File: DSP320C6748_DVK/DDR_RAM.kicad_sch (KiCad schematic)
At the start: 66 parts, among them IC13 W972GG6KB-25

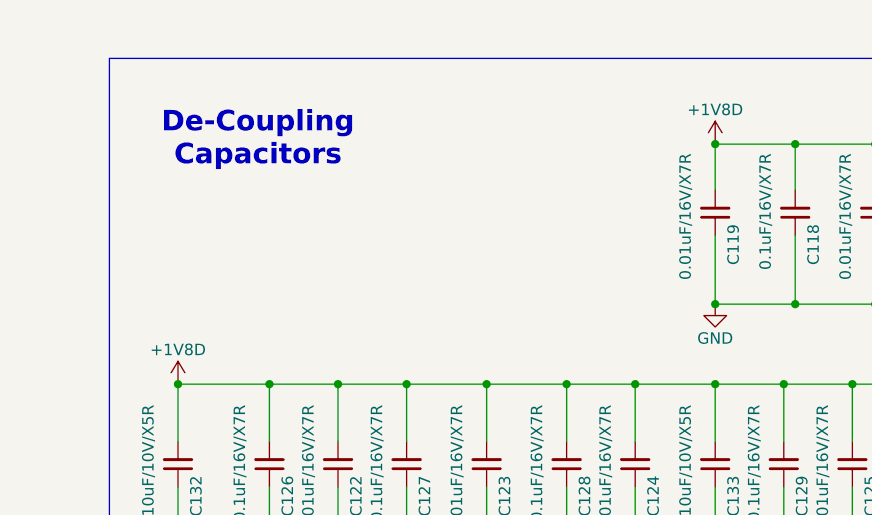
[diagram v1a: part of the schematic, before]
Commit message: NAND Flash circuit and Power Testpoints added
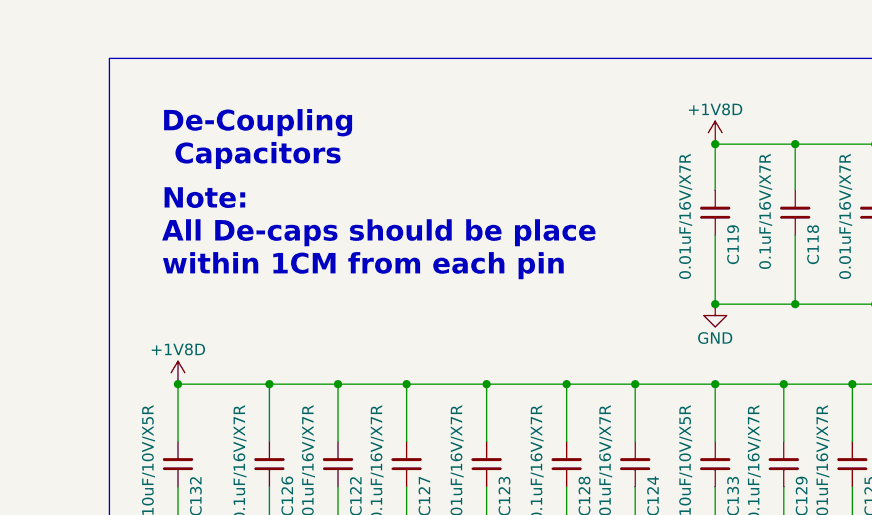
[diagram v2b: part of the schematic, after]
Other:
- note added: "Note: All De-caps should be place within 1CM from each pin"
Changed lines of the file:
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@@
+		)
+	)
+	(text "Note:\nAll De-caps should be place\nwithin 1CM from each pin"
+		(exclude_from_sim no)
+		(at 164.592 41.656 0)
+		(effects
+			(font
+				(size 2.27 2.27)
+				(thickness 0.454)
+				(bold yes)
+			)
+			(justify left)
 		)
 	)

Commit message: Whole Schematic Reannotation Done
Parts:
- renumbered C117 to C122, C116 to C123, C132 to C124, C126 to C125, C122 to C126, C123 to C128, C128 to C129, C124 to C130, C119 to C131, C133 to C132, C129 to C133, C118 to C134, C125 to C135, C121 to C136, C130 to C137, C120 to C138, C131 to C139, IC13 to IC14, R178 to R104, R163 to R105, R147 to R106, R149 to R107, R164 to R108, R165 to R109, R166 to R110, R167 to R111, R168 to R112, R169 to R113, R170 to R114, R171 to R115, R146 to R116, R148 to R117, R172 to R118, R173 to R119, R174 to R120, R177 to R121, R175 to R122, R161 to R123, R162 to R124, R176 to R125, R150 to R126, R151 to R127, R153 to R128, R154 to R129, R152 to R130, R157 to R131, R158 to R132, R159 to R133, R160 to R134, R155 to R135, R156 to R136, R132 to R137, R133 to R138, R134 to R139, R135 to R140, R136 to R141, R137 to R142, R138 to R143, R139 to R144, R140 to R145, R141 to R146, R142 to R147, R143 to R148, R144 to R149, R145 to R150

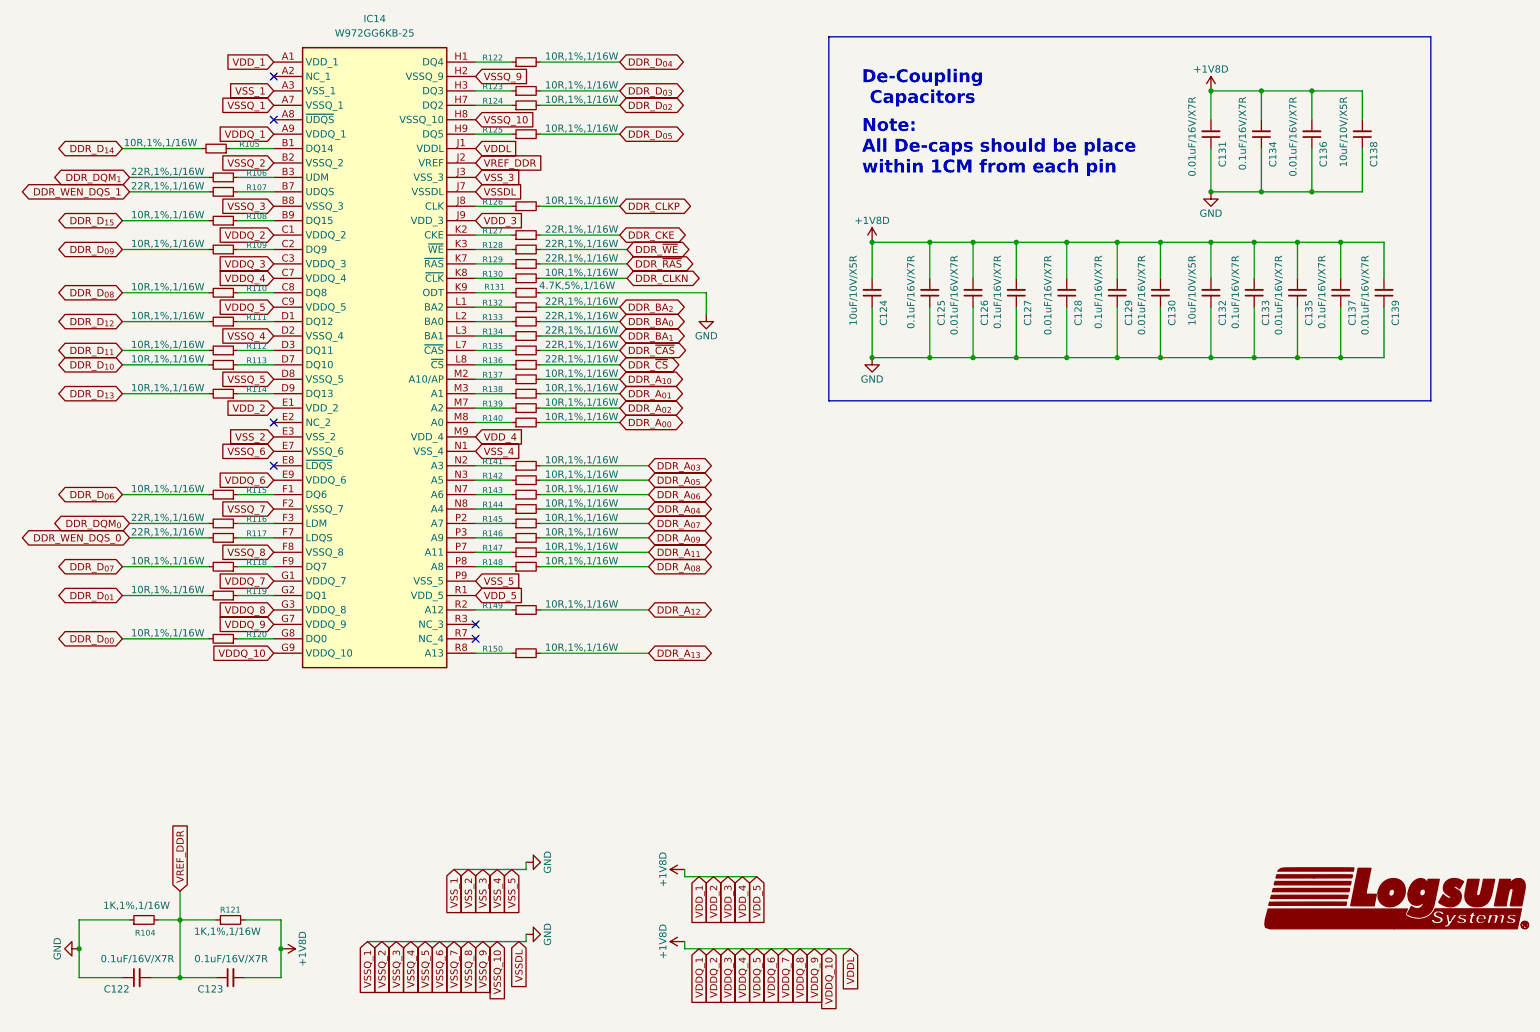
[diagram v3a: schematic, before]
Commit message: DC jack Replaced With Type-C, ADC and RTC section added
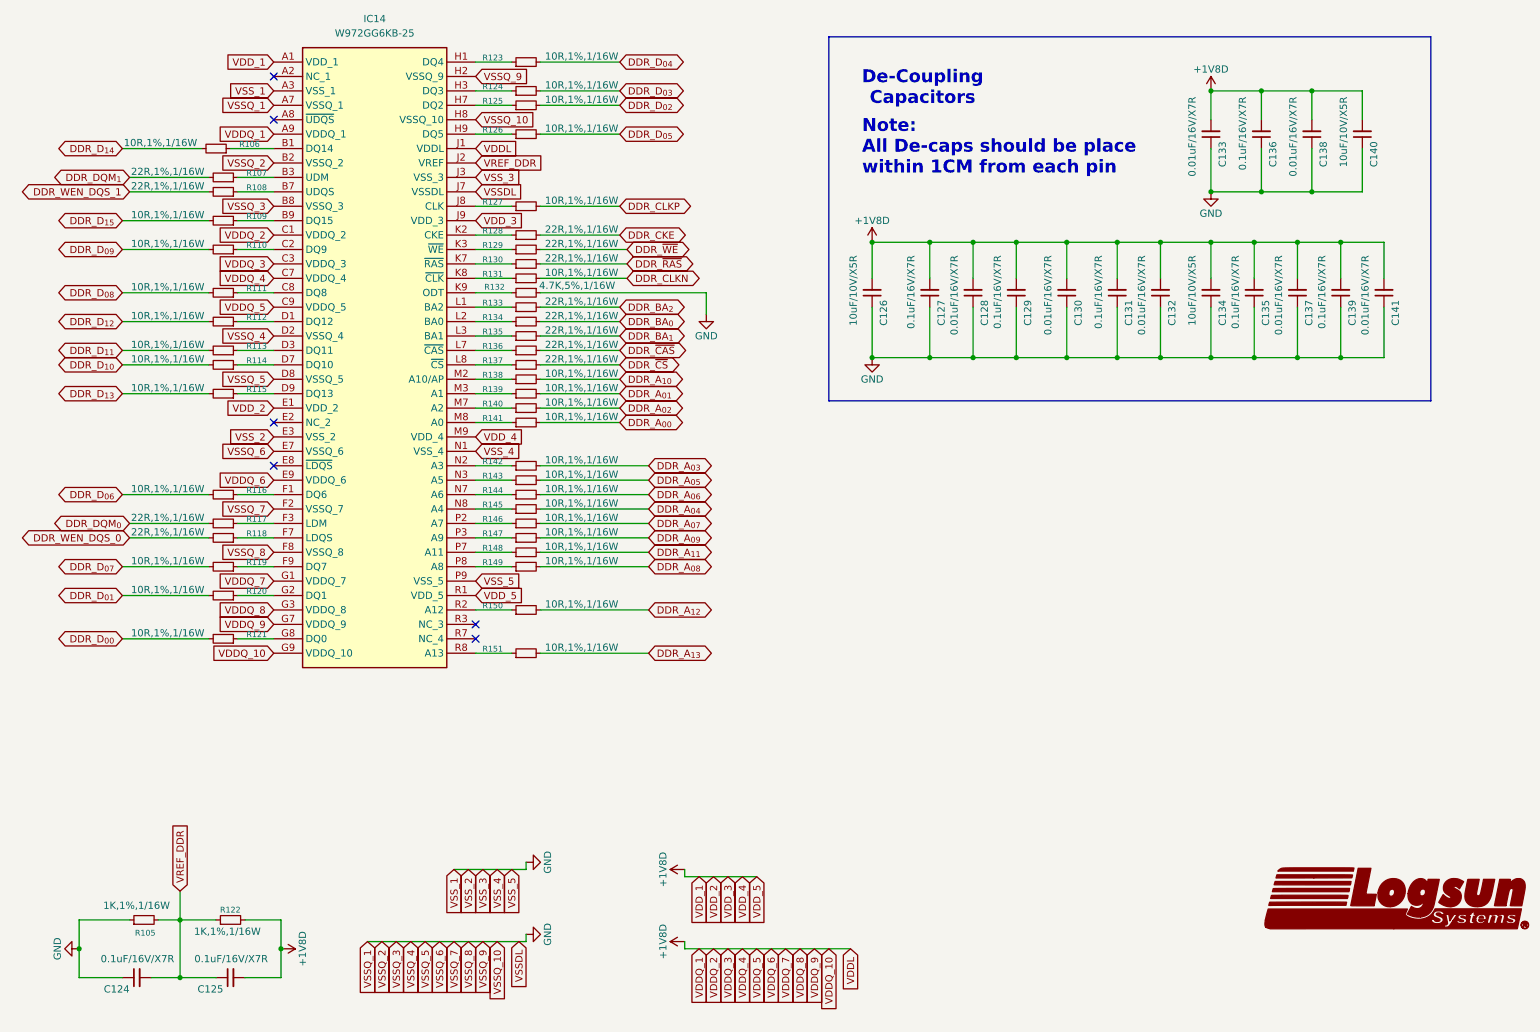
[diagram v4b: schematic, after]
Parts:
- renumbered C122 to C124, C123 to C125, C124 to C126, C125 to C127, C126 to C128, C127 to C129, C128 to C130, C129 to C131, C130 to C132, C131 to C133, C132 to C134, C133 to C135, C134 to C136, C135 to C137, C136 to C138, C137 to C139, C138 to C140, C139 to C141, R104 to R105, R105 to R106, R106 to R107, R107 to R108, R108 to R109, R109 to R110, R110 to R111, R111 to R112, R112 to R113, R113 to R114, R114 to R115, R115 to R116, R116 to R117, R117 to R118, R118 to R119, R119 to R120, R120 to R121, R121 to R122, R122 to R123, R123 to R124, R124 to R125, R125 to R126, R126 to R127, R127 to R128, R128 to R129, R129 to R130, R130 to R131, R131 to R132, R132 to R133, R133 to R134, R134 to R135, R135 to R136, R136 to R137, R137 to R138, R138 to R139, R139 to R140, R140 to R141, R141 to R142, R142 to R143, R143 to R144, R144 to R145, R145 to R146, R146 to R147, R147 to R148, R148 to R149, R149 to R150, R150 to R151

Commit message: Scheamtic Re-annotation done, Some footprints assigned
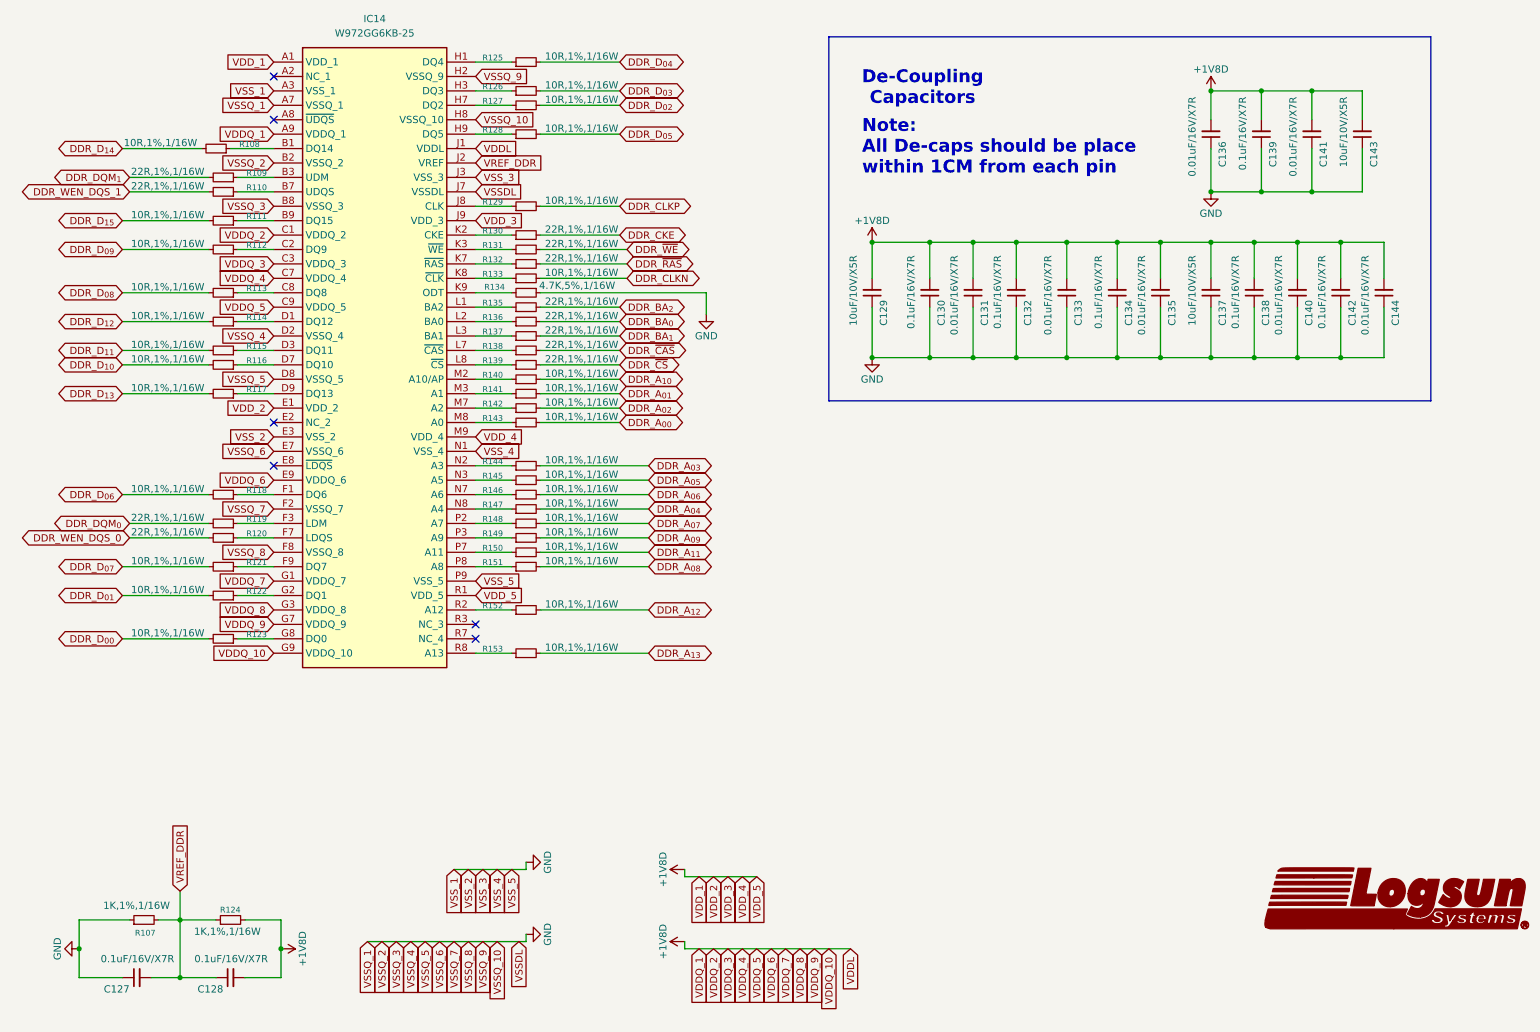
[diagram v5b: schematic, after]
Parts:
- C127: renamed from C124; footprint (none) -> Capacitor_SMD:C_0603_1608Metric_Pad1.08x0.95mm_HandSolder
- C128: renamed from C125; footprint (none) -> Capacitor_SMD:C_0603_1608Metric_Pad1.08x0.95mm_HandSolder
- C129: renamed from C126; footprint (none) -> Capacitor_SMD:C_0603_1608Metric_Pad1.08x0.95mm_HandSolder
- C130: renamed from C127; footprint (none) -> Capacitor_SMD:C_0603_1608Metric_Pad1.08x0.95mm_HandSolder
- C131: renamed from C128; footprint (none) -> Capacitor_SMD:C_0603_1608Metric_Pad1.08x0.95mm_HandSolder
- C132: renamed from C129; footprint (none) -> Capacitor_SMD:C_0603_1608Metric_Pad1.08x0.95mm_HandSolder
- C133: renamed from C130; footprint (none) -> Capacitor_SMD:C_0603_1608Metric_Pad1.08x0.95mm_HandSolder
- C134: renamed from C131; footprint (none) -> Capacitor_SMD:C_0603_1608Metric_Pad1.08x0.95mm_HandSolder
- C135: renamed from C132; footprint (none) -> Capacitor_SMD:C_0603_1608Metric_Pad1.08x0.95mm_HandSolder
- C136: renamed from C133; footprint (none) -> Capacitor_SMD:C_0603_1608Metric_Pad1.08x0.95mm_HandSolder
- C137: renamed from C134; footprint (none) -> Capacitor_SMD:C_0603_1608Metric_Pad1.08x0.95mm_HandSolder
- C138: renamed from C135; footprint (none) -> Capacitor_SMD:C_0603_1608Metric_Pad1.08x0.95mm_HandSolder
- C139: renamed from C136; footprint (none) -> Capacitor_SMD:C_0603_1608Metric_Pad1.08x0.95mm_HandSolder
- C140: renamed from C137; footprint (none) -> Capacitor_SMD:C_0603_1608Metric_Pad1.08x0.95mm_HandSolder
- C141: renamed from C138; footprint (none) -> Capacitor_SMD:C_0603_1608Metric_Pad1.08x0.95mm_HandSolder
- C142: renamed from C139; footprint (none) -> Capacitor_SMD:C_0603_1608Metric_Pad1.08x0.95mm_HandSolder
- C143: renamed from C140; footprint (none) -> Capacitor_SMD:C_0603_1608Metric_Pad1.08x0.95mm_HandSolder
- C144: renamed from C141; footprint (none) -> Capacitor_SMD:C_0603_1608Metric_Pad1.08x0.95mm_HandSolder
- R107: renamed from R105; footprint (none) -> Resistor_SMD:R_0603_1608Metric_Pad0.98x0.95mm_HandSolder
- R108: renamed from R106; footprint (none) -> Resistor_SMD:R_0603_1608Metric_Pad0.98x0.95mm_HandSolder
- R109: renamed from R107; footprint (none) -> Resistor_SMD:R_0603_1608Metric_Pad0.98x0.95mm_HandSolder
- R110: renamed from R108; footprint (none) -> Resistor_SMD:R_0603_1608Metric_Pad0.98x0.95mm_HandSolder
- R111: renamed from R109; footprint (none) -> Resistor_SMD:R_0603_1608Metric_Pad0.98x0.95mm_HandSolder
- R112: renamed from R110; footprint (none) -> Resistor_SMD:R_0603_1608Metric_Pad0.98x0.95mm_HandSolder
- R113: renamed from R111; footprint (none) -> Resistor_SMD:R_0603_1608Metric_Pad0.98x0.95mm_HandSolder
- R114: renamed from R112; footprint (none) -> Resistor_SMD:R_0603_1608Metric_Pad0.98x0.95mm_HandSolder
- R115: renamed from R113; footprint (none) -> Resistor_SMD:R_0603_1608Metric_Pad0.98x0.95mm_HandSolder
- R116: renamed from R114; footprint (none) -> Resistor_SMD:R_0603_1608Metric_Pad0.98x0.95mm_HandSolder
- R117: renamed from R115; footprint (none) -> Resistor_SMD:R_0603_1608Metric_Pad0.98x0.95mm_HandSolder
- R118: renamed from R116; footprint (none) -> Resistor_SMD:R_0603_1608Metric_Pad0.98x0.95mm_HandSolder
- R119: renamed from R117; footprint (none) -> Resistor_SMD:R_0603_1608Metric_Pad0.98x0.95mm_HandSolder
- R120: renamed from R118; footprint (none) -> Resistor_SMD:R_0603_1608Metric_Pad0.98x0.95mm_HandSolder
- R121: renamed from R119; footprint (none) -> Resistor_SMD:R_0603_1608Metric_Pad0.98x0.95mm_HandSolder
- R122: renamed from R120; footprint (none) -> Resistor_SMD:R_0603_1608Metric_Pad0.98x0.95mm_HandSolder
- R123: renamed from R121; footprint (none) -> Resistor_SMD:R_0603_1608Metric_Pad0.98x0.95mm_HandSolder
- R124: renamed from R122; footprint (none) -> Resistor_SMD:R_0603_1608Metric_Pad0.98x0.95mm_HandSolder
- R125: renamed from R123; footprint (none) -> Resistor_SMD:R_0603_1608Metric_Pad0.98x0.95mm_HandSolder
- R126: renamed from R124; footprint (none) -> Resistor_SMD:R_0603_1608Metric_Pad0.98x0.95mm_HandSolder
- R127: renamed from R125; footprint (none) -> Resistor_SMD:R_0603_1608Metric_Pad0.98x0.95mm_HandSolder
- R128: renamed from R126; footprint (none) -> Resistor_SMD:R_0603_1608Metric_Pad0.98x0.95mm_HandSolder
- R129: renamed from R127; footprint (none) -> Resistor_SMD:R_0603_1608Metric_Pad0.98x0.95mm_HandSolder
- R130: renamed from R128; footprint (none) -> Resistor_SMD:R_0603_1608Metric_Pad0.98x0.95mm_HandSolder
- R131: renamed from R129; footprint (none) -> Resistor_SMD:R_0603_1608Metric_Pad0.98x0.95mm_HandSolder
- R132: renamed from R130; footprint (none) -> Resistor_SMD:R_0603_1608Metric_Pad0.98x0.95mm_HandSolder
- R133: renamed from R131; footprint (none) -> Resistor_SMD:R_0603_1608Metric_Pad0.98x0.95mm_HandSolder
- R134: renamed from R132; footprint (none) -> Resistor_SMD:R_0603_1608Metric_Pad0.98x0.95mm_HandSolder
- R135: renamed from R133; footprint (none) -> Resistor_SMD:R_0603_1608Metric_Pad0.98x0.95mm_HandSolder
- R136: renamed from R134; footprint (none) -> Resistor_SMD:R_0603_1608Metric_Pad0.98x0.95mm_HandSolder
- R137: renamed from R135; footprint (none) -> Resistor_SMD:R_0603_1608Metric_Pad0.98x0.95mm_HandSolder
- R138: renamed from R136; footprint (none) -> Resistor_SMD:R_0603_1608Metric_Pad0.98x0.95mm_HandSolder
- R139: renamed from R137; footprint (none) -> Resistor_SMD:R_0603_1608Metric_Pad0.98x0.95mm_HandSolder
- R140: renamed from R138; footprint (none) -> Resistor_SMD:R_0603_1608Metric_Pad0.98x0.95mm_HandSolder
- R141: renamed from R139; footprint (none) -> Resistor_SMD:R_0603_1608Metric_Pad0.98x0.95mm_HandSolder
- R142: renamed from R140; footprint (none) -> Resistor_SMD:R_0603_1608Metric_Pad0.98x0.95mm_HandSolder
- R143: renamed from R141; footprint (none) -> Resistor_SMD:R_0603_1608Metric_Pad0.98x0.95mm_HandSolder
- R144: renamed from R142; footprint (none) -> Resistor_SMD:R_0603_1608Metric_Pad0.98x0.95mm_HandSolder
- R145: renamed from R143; footprint (none) -> Resistor_SMD:R_0603_1608Metric_Pad0.98x0.95mm_HandSolder
- R146: renamed from R144; footprint (none) -> Resistor_SMD:R_0603_1608Metric_Pad0.98x0.95mm_HandSolder
- R147: renamed from R145; footprint (none) -> Resistor_SMD:R_0603_1608Metric_Pad0.98x0.95mm_HandSolder
- R148: renamed from R146; footprint (none) -> Resistor_SMD:R_0603_1608Metric_Pad0.98x0.95mm_HandSolder
- R149: renamed from R147; footprint (none) -> Resistor_SMD:R_0603_1608Metric_Pad0.98x0.95mm_HandSolder
- R150: renamed from R148; footprint (none) -> Resistor_SMD:R_0603_1608Metric_Pad0.98x0.95mm_HandSolder
- R151: renamed from R149; footprint (none) -> Resistor_SMD:R_0603_1608Metric_Pad0.98x0.95mm_HandSolder
- R152: renamed from R150; footprint (none) -> Resistor_SMD:R_0603_1608Metric_Pad0.98x0.95mm_HandSolder
- R153: renamed from R151; footprint (none) -> Resistor_SMD:R_0603_1608Metric_Pad0.98x0.95mm_HandSolder
